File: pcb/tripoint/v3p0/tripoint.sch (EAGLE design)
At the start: 68 parts, among them J2 TC2030-JLINK-NL, T1 HHM1595A1, U1 STM32F091CC, U2 DW1000, U3 SKY13317, U4 LXDC2HN18A, X1 38.4M, X2 16M

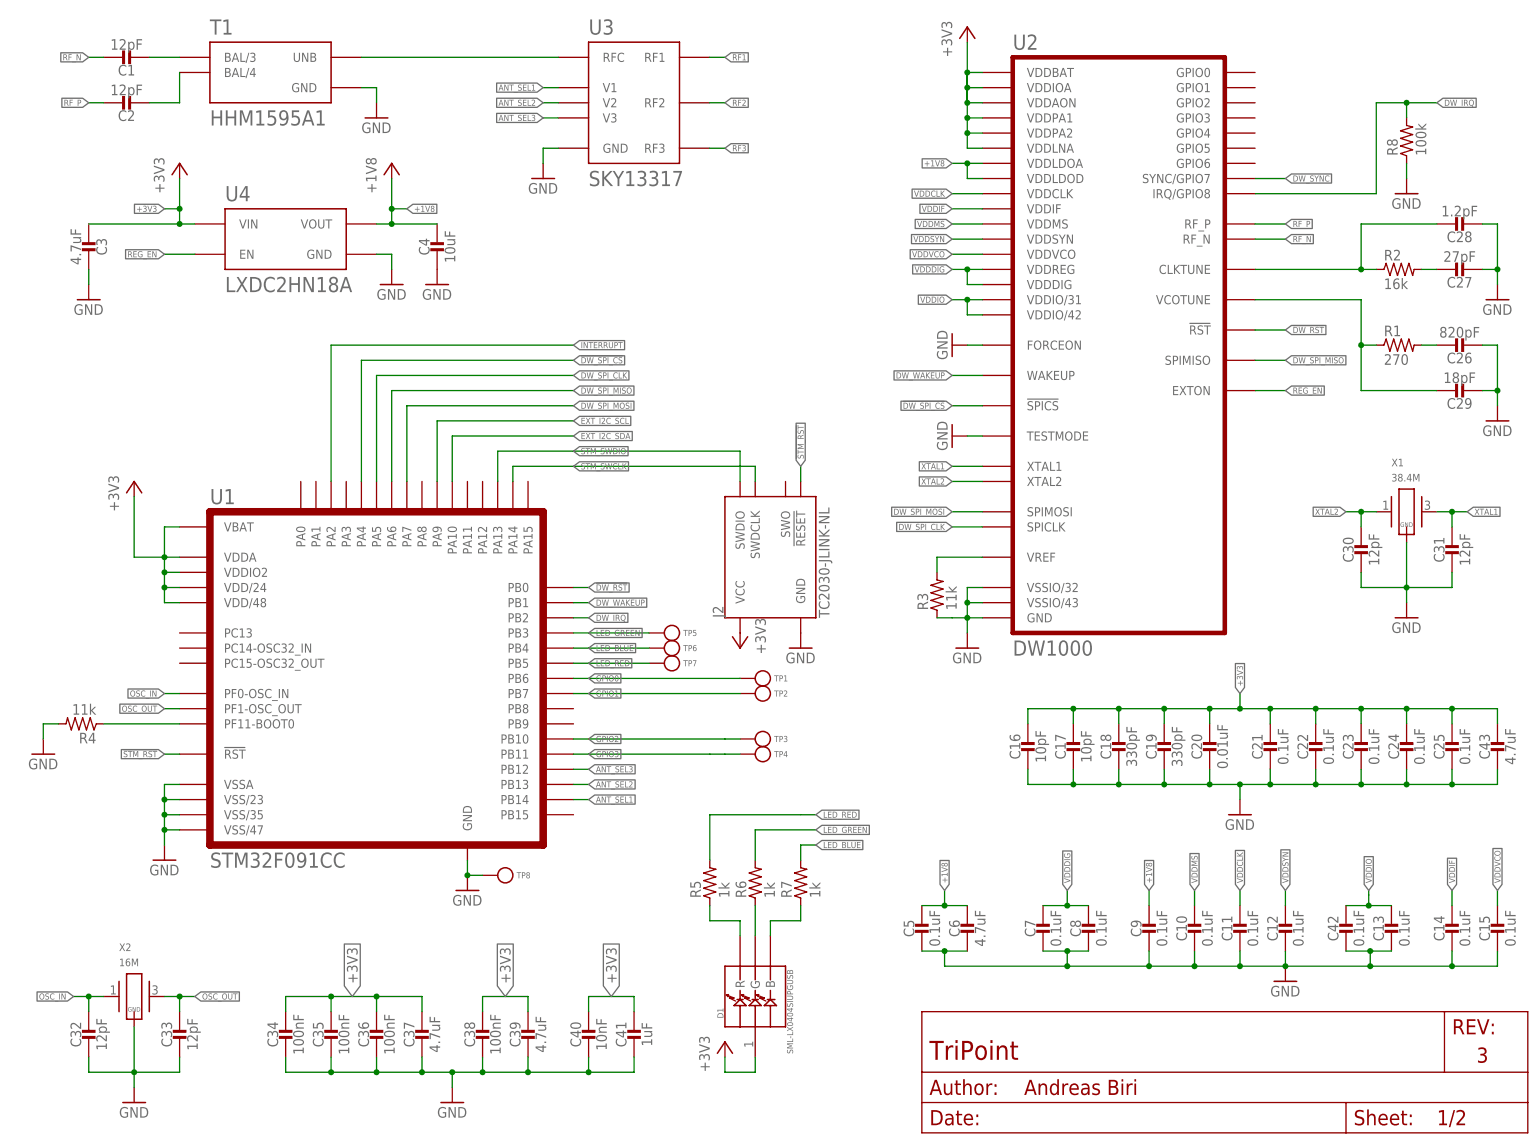
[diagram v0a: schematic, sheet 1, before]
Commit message: added second pass of TriPoint schematic and component positions
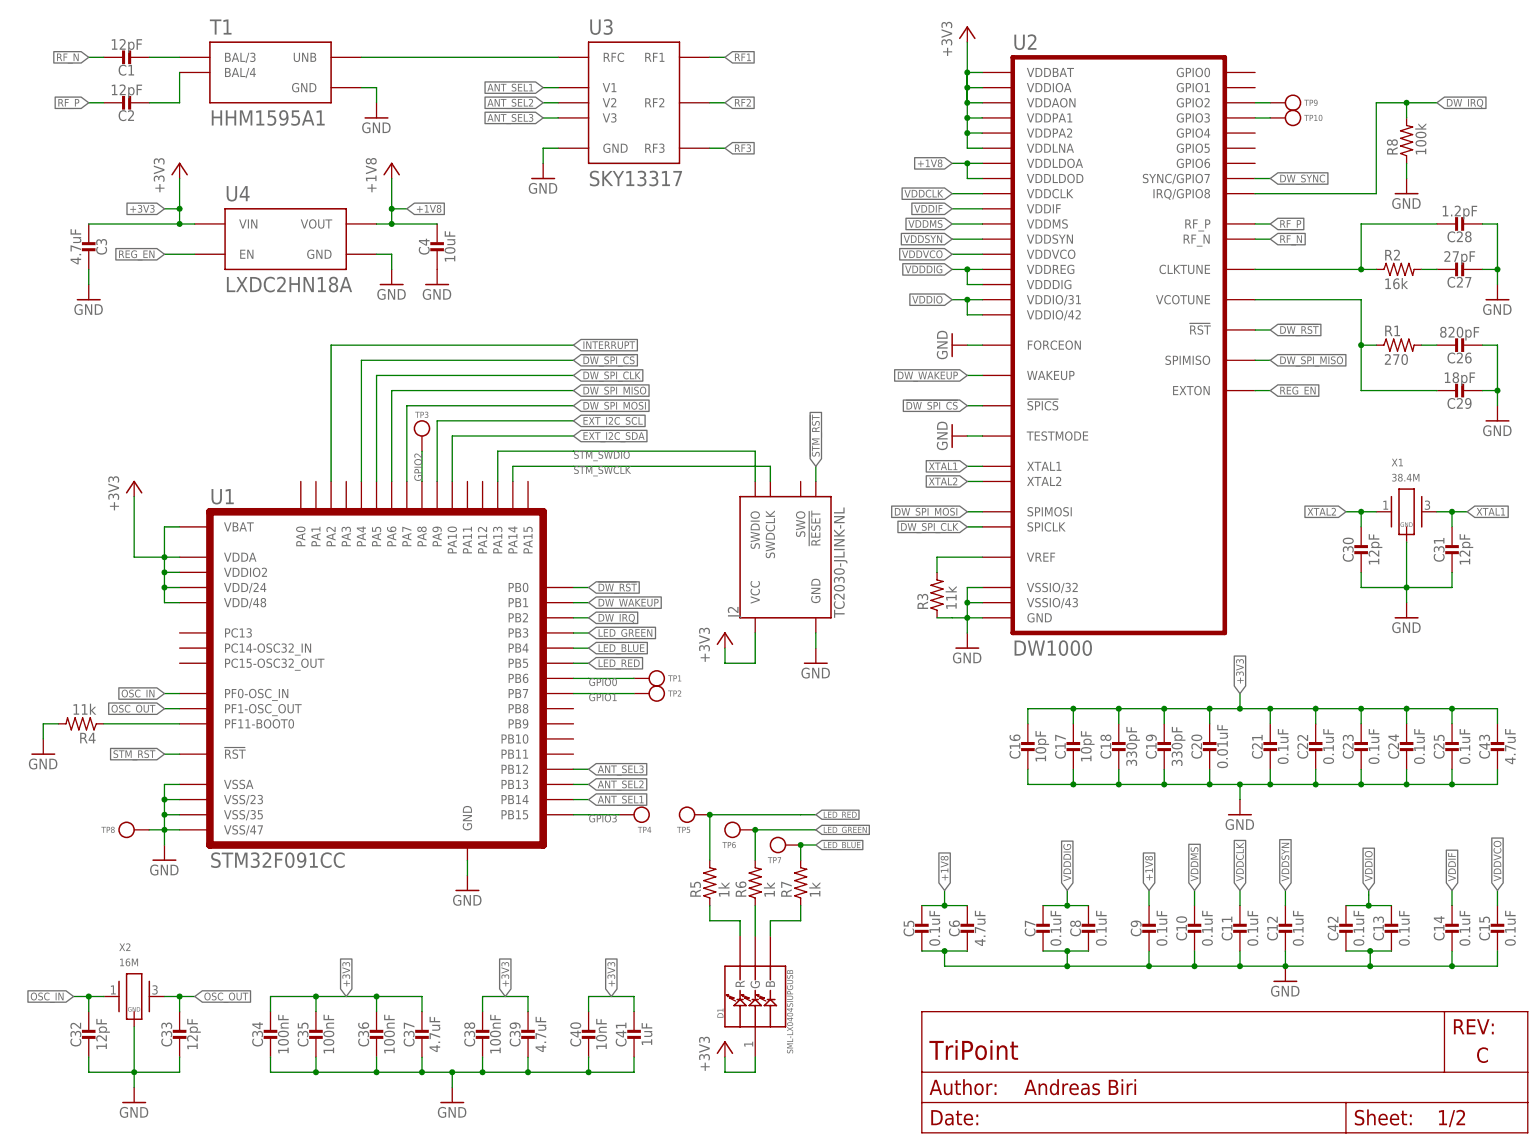
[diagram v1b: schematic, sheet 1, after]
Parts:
- added TP10, TP9: TEST-POINT, headers:TEST-POINT
- C10, C11, C12, C13, C14, C15, C16, C17, C18, C19, C20, C21, C22, C23, C24, C25, C26, C27, C28, C29, C30, C31, C32, C33, C34, C35, C36, C37, C38, C39, C40, C41, C42, C5, C7, C8, C9: device passives:CAPACITOR0201_CAP -> passives:CAPACITOR0402_CAP
- C3, C43, C6: device passives:CAPACITOR0603_CAP -> passives:CAPACITOR0402_CAP
- R1, R2, R3, R4, R8: device passives:RESISTOR0201_RES -> passives:RESISTOR0402_RES
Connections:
- new net N$13: TP9.TESTPOINT, U2.GPIO2
- new net N$14: TP10.TESTPOINT, U2.GPIO3
- net GPIO2: now also U1.PA8; no longer U1.PB10
- net GPIO3: now also U1.PB15; no longer U1.PB11
- net LED_BLUE: now also TP7.TESTPOINT; no longer TP6.TESTPOINT
- net LED_GREEN: now also TP6.TESTPOINT; no longer TP5.TESTPOINT
- net LED_RED: now also TP5.TESTPOINT; no longer TP7.TESTPOINT
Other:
- note added: "Note: Additional I2C pull-up resistors required to +3V3"
- note added: "VDD/24"
- note added: "VDD/48"
- note removed: "Note: Additional I2C pull-up resistors required"
- note removed: "VDD"
- moved on the sheet: C34, C35, J2, TP1, TP2, TP3, TP4, TP5, TP6, TP7, TP8

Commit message: finished second pass of TriPoint
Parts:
- C38: value 100nF -> 4.7uF
- C39: value 4.7uF -> 100nF
- C40: value 10nF -> 1uF
- C41: value 1uF -> 10nF
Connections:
- net LED_BLUE: no longer TP7.TESTPOINT
- net LED_GREEN: now also U1.PB5; no longer TP6.TESTPOINT, U1.PB3
- net LED_RED: now also U1.PB3; no longer TP5.TESTPOINT, U1.PB5
- net N$10: now also TP5.TESTPOINT
- net N$11: now also TP7.TESTPOINT
- net N$12: now also TP6.TESTPOINT
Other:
- moved on the sheet: R5, R6, R7, TP5, TP6, TP7
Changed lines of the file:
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@@
 <part name="C36" library="passives" deviceset="CAPACITOR" device="0402_CAP" value="100nF"/>
 <part name="C37" library="passives" deviceset="CAPACITOR" device="0402_CAP" value="4.7uF"/>
-<part name="C38" library="passives" deviceset="CAPACITOR" device="0402_CAP" value="100nF"/>
-<part name="C39" library="passives" deviceset="CAPACITOR" device="0402_CAP" value="4.7uF"/>
-<part name="C40" library="passives" deviceset="CAPACITOR" device="0402_CAP" value="10nF"/>
-<part name="C41" library="passives" deviceset="CAPACITOR" device="0402_CAP" value="1uF"/>
+<part name="C38" library="passives" deviceset="CAPACITOR" device="0402_CAP" value="4.7uF"/>
+<part name="C39" library="passives" deviceset="CAPACITOR" device="0402_CAP" value="100nF"/>
+<part name="C40" library="passives" deviceset="CAPACITOR" device="0402_CAP" value="1uF"/>
+<part name="C41" library="passives" deviceset="CAPACITOR" device="0402_CAP" value="10nF"/>
 <part name="SUPPLY19" library="regulators" deviceset="GND" device=""/>
 <part name="R4" library="passives" deviceset="RESISTOR" device="0402_RES" value="11k"/>
@@
 <text x="114.3" y="73.66" size="0.762" layer="98">PC
 Test Points</text>
-<text x="114.808" y="56.134" size="0.762" layer="98">Pad
+<text x="101.6" y="47.498" size="0.762" layer="98">Pad
 Test Points</text>
 <text x="129.54" y="30.48" size="2.032" layer="98">LED</text>
@@
 <instance part="SUPPLY22" gate="G1" x="134.62" y="78.74"/>
 <instance part="+3V4" gate="P1" x="119.38" y="83.82"/>
-<instance part="R5" gate="G$1" x="116.84" y="43.18" rot="R90"/>
-<instance part="R6" gate="G$1" x="124.46" y="43.18" rot="R90"/>
+<instance part="R5" gate="G$1" x="114.3" y="50.8" rot="R90"/>
+<instance part="R6" gate="G$1" x="124.46" y="50.8" rot="R90"/>
 <instance part="D1" gate="G$1" x="124.46" y="22.86" rot="R90"/>
-<instance part="R7" gate="G$1" x="132.08" y="43.18" rot="R90"/>
+<instance part="R7" gate="G$1" x="134.62" y="50.8" rot="R90"/>
 <instance part="TP1" gate="G$1" x="106.68" y="76.2" rot="R180"/>
 <instance part="TP2" gate="G$1" x="106.68" y="73.66" rot="R180"/>
@@
 <instance part="C42" gate="G$1" x="223.52" y="35.56"/>
 <instance part="C43" gate="G$1" x="248.92" y="66.04"/>
-<instance part="TP5" gate="G$1" x="114.3" y="53.34" smashed="yes">
-<attribute name="NAME" x="113.665" y="50.8" size="1.016" layer="95" ratio="12" align="center-right"/>
+<instance part="TP5" gate="G$1" x="129.54" y="40.64" smashed="yes" rot="R180">
+<attribute name="NAME" x="130.175" y="38.1" size="1.016" layer="95" ratio="12" rot="R180" align="center-right"/>
 </instance>
-<instance part="TP6" gate="G$1" x="121.92" y="50.8" smashed="yes">
-<attribute name="NAME" x="121.285" y="48.26" size="1.016" layer="95" ratio="12" align="center-right"/>
+<instance part="TP6" gate="G$1" x="119.38" y="40.64" smashed="yes" rot="R180">
+<attribute name="NAME" x="120.015" y="38.1" size="1.016" layer="95" ratio="12" rot="R180" align="center-right"/>
 </instance>
-<instance part="TP7" gate="G$1" x="129.54" y="48.26" smashed="yes">
-<attribute name="NAME" x="128.905" y="45.72" size="1.016" layer="95" ratio="12" align="center-right"/>
+<instance part="TP7" gate="G$1" x="139.7" y="40.64" smashed="yes" rot="R180">
+<attribute name="NAME" x="140.335" y="38.1" size="1.016" layer="95" ratio="12" rot="R180" align="center-right"/>
 </instance>
 <instance part="TP8" gate="G$1" x="20.32" y="50.8"/>
@@
 <pinref part="R6" gate="G$1" pin="1"/>
 <pinref part="D1" gate="G$1" pin="G"/>
-<wire x1="124.46" y1="38.1" x2="124.46" y2="33.02" width="0.1524" layer="91"/>
+<wire x1="124.46" y1="45.72" x2="124.46" y2="40.64" width="0.1524" layer="91"/>
+<pinref part="TP5" gate="G$1" pin="TESTPOINT"/>
+<wire x1="124.46" y1="40.64" x2="124.46" y2="33.02" width="0.1524" layer="91"/>
+<wire x1="127" y1="40.64" x2="124.46" y2="40.64" width="0.1524" layer="91"/>
+<junction x="124.46" y="40.64"/>
 </segment>
 </net>
@@
 <segment>
 <pinref part="R7" gate="G$1" pin="1"/>
-<wire x1="132.08" y1="38.1" x2="132.08" y2="35.56" width="0.1524" layer="91"/>
-<wire x1="132.08" y1="35.56" x2="127" y2="35.56" width="0.1524" layer="91"/>
+<wire x1="134.62" y1="45.72" x2="134.62" y2="40.64" width="0.1524" layer="91"/>
+<wire x1="134.62" y1="40.64" x2="134.62" y2="35.56" width="0.1524" layer="91"/>
+<wire x1="134.62" y1="35.56" x2="127" y2="35.56" width="0.1524" layer="91"/>
 <pinref part="D1" gate="G$1" pin="B"/>
 <wire x1="127" y1="35.56" x2="127" y2="33.02" width="0.1524" layer="91"/>
+<pinref part="TP7" gate="G$1" pin="TESTPOINT"/>
+<wire x1="137.16" y1="40.64" x2="134.62" y2="40.64" width="0.1524" layer="91"/>
+<junction x="134.62" y="40.64"/>
 </segment>
 </net>
@@
 <segment>
 <pinref part="R5" gate="G$1" pin="1"/>
-<wire x1="116.84" y1="38.1" x2="116.84" y2="35.56" width="0.1524" layer="91"/>
-<wire x1="116.84" y1="35.56" x2="121.92" y2="35.56" width="0.1524" layer="91"/>
+<wire x1="114.3" y1="45.72" x2="114.3" y2="40.64" width="0.1524" layer="91"/>
+<wire x1="114.3" y1="40.64" x2="114.3" y2="35.56" width="0.1524" layer="91"/>
+<wire x1="114.3" y1="35.56" x2="121.92" y2="35.56" width="0.1524" layer="91"/>
 <pinref part="D1" gate="G$1" pin="R"/>
 <wire x1="121.92" y1="35.56" x2="121.92" y2="33.02" width="0.1524" layer="91"/>
+<pinref part="TP6" gate="G$1" pin="TESTPOINT"/>
+<wire x1="116.84" y1="40.64" x2="114.3" y2="40.64" width="0.1524" layer="91"/>
+<junction x="114.3" y="40.64"/>
 </segment>
 </net>
@@
 <net name="LED_RED" class="0">
 <segment>
+<wire x1="132.08" y1="60.96" x2="134.62" y2="60.96" width="0.1524" layer="91"/>
+<label x="134.62" y="60.96" size="1.016" layer="95" xref="yes"/>
 <pinref part="R5" gate="G$1" pin="2"/>
-<wire x1="116.84" y1="45.72" x2="116.84" y2="53.34" width="0.1524" layer="91"/>
-<wire x1="116.84" y1="53.34" x2="132.08" y2="53.34" width="0.1524" layer="91"/>
-<wire x1="132.08" y1="53.34" x2="134.62" y2="53.34" width="0.1524" layer="91"/>
-<label x="134.62" y="53.34" size="1.016" layer="95" xref="yes"/>
-<pinref part="TP5" gate="G$1" pin="TESTPOINT"/>
-<junction x="116.84" y="53.34"/>
-</segment>
+<wire x1="114.3" y1="53.34" x2="114.3" y2="60.96" width="0.1524" layer="91"/>
+<wire x1="114.3" y1="60.96" x2="132.08" y2="60.96" width="0.1524" layer="91"/>
+</segment>
+<segment>
+<pinref part="U1" gate="U1" pin="PB3"/>
+<wire x1="93.98" y1="83.82" x2="96.52" y2="83.82" width="0.1524" layer="91"/>
+<label x="96.52" y="83.82" size="1.27" layer="95" xref="yes"/>
+</segment>
+</net>
+<net name="LED_BLUE" class="0">
+<segment>
+<pinref part="U1" gate="U1" pin="PB4"/>
+<wire x1="93.98" y1="81.28" x2="96.52" y2="81.28" width="0.1524" layer="91"/>
+<label x="96.52" y="81.28" size="1.27" layer="95" xref="yes"/>
+</segment>
+<segment>
+<pinref part="R7" gate="G$1" pin="2"/>
+<wire x1="134.62" y1="53.34" x2="134.62" y2="55.88" width="0.1524" layer="91"/>
+<label x="134.62" y="55.88" size="1.016" layer="95" xref="yes"/>
+</segment>
+</net>
+<net name="LED_GREEN" class="0">
 <segment>
 <pinref part="U1" gate="U1" pin="PB5"/>
@@
 <label x="96.52" y="78.74" size="1.27" layer="95" xref="yes"/>
 </segment>
-</net>
-<net name="LED_BLUE" class="0">
-<segment>
-<pinref part="R7" gate="G$1" pin="2"/>
-<wire x1="132.08" y1="45.72" x2="132.08" y2="48.26" width="0.1524" layer="91"/>
-<wire x1="132.08" y1="48.26" x2="134.62" y2="48.26" width="0.1524" layer="91"/>
-<label x="134.62" y="48.26" size="1.016" layer="95" xref="yes"/>
-<pinref part="TP7" gate="G$1" pin="TESTPOINT"/>
-<junction x="132.08" y="48.26"/>
-</segment>
-<segment>
-<pinref part="U1" gate="U1" pin="PB4"/>
-<wire x1="93.98" y1="81.28" x2="96.52" y2="81.28" width="0.1524" layer="91"/>
-<label x="96.52" y="81.28" size="1.27" layer="95" xref="yes"/>
-</segment>
-</net>
-<net name="LED_GREEN" class="0">
 <segment>
 <pinref part="R6" gate="G$1" pin="2"/>
-<wire x1="124.46" y1="45.72" x2="124.46" y2="50.8" width="0.1524" layer="91"/>
-<wire x1="124.46" y1="50.8" x2="134.62" y2="50.8" width="0.1524" layer="91"/>
-<label x="134.62" y="50.8" size="1.016" layer="95" xref="yes"/>
-<pinref part="TP6" gate="G$1" pin="TESTPOINT"/>
-<junction x="124.46" y="50.8"/>
-</segment>
-<segment>
-<pinref part="U1" gate="U1" pin="PB3"/>
-<wire x1="93.98" y1="83.82" x2="96.52" y2="83.82" width="0.1524" layer="91"/>
-<label x="96.52" y="83.82" size="1.27" layer="95" xref="yes"/>
-</segment>
-</net>
+<wire x1="124.46" y1="53.34" x2="124.46" y2="58.42" width="0.1524" layer="91"/>
+<wire x1="124.46" y1="58.42" x2="134.62" y2="58.42" width="0.1524" layer="91"/>
+<label x="134.62" y="58.42" size="1.016" layer="95" xref="yes"/>
+</segment>
+</net>

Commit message: finished third pass, SquarePoint it is
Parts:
- R3: value 11k -> 11k 1%
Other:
- note added: "Antennas"
- note added: "Be aware that the DecaWave is very sensitive regarding its power supply. We suggest using the "MAX8887EZK33+T" from Maxim Integrated. You can find a reference layout at github.com/lab11/polypoint/pcb/tritag."
- note added: "Guarantee 120° offset in-between antennas to maximize polarization difference and antenna diversity RF traces should respect the keepout zones and be surrounded by a via shield. Furthermore, try to keep them as short and straight as possible"
- note added: "Power Supply"
- note added: "Signals"
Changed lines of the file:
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@@
 <part name="R1" library="passives" deviceset="RESISTOR" device="0402_RES" value="270"/>
 <part name="R2" library="passives" deviceset="RESISTOR" device="0402_RES" value="16k"/>
-<part name="R3" library="passives" deviceset="RESISTOR" device="0402_RES" value="11k"/>
+<part name="R3" library="passives" deviceset="RESISTOR" device="0402_RES" value="11k 1%"/>
 <part name="C26" library="passives" deviceset="CAPACITOR" device="0402_CAP" value="820pF"/>
 <part name="C27" library="passives" deviceset="CAPACITOR" device="0402_CAP" value="27pF"/>
@@
 <text x="35.56" y="149.86" size="2.54" layer="98">The following signals must be integrated into all designs using the design block:</text>
 <text x="86.36" y="134.62" size="2.54" layer="98">Note: Additional I2C pull-up resistors required to +3V3</text>
+<text x="78.74" y="60.96" size="2.54" layer="98">Be aware that the DecaWave is very sensitive regarding its power supply.
+We suggest using the "MAX8887EZK33+T" from Maxim Integrated.
+You can find a reference layout at github.com/lab11/polypoint/pcb/tritag.</text>
+<text x="7.62" y="101.6" size="3.556" layer="98">Antennas</text>
+<text x="78.74" y="88.9" size="2.54" layer="98">Guarantee 120° offset in-between antennas to maximize  polarization difference and antenna diversity
+RF traces should respect the keepout zones and be surrounded by a via shield.
+Furthermore, try to keep them as short and straight as possible</text>
+<text x="7.62" y="73.66" size="3.556" layer="98">Power Supply</text>
+<text x="7.62" y="137.16" size="3.556" layer="98">Signals</text>
 </plain>
 <instances>
@@
 <net name="RF1" class="0">
 <segment>
-<wire x1="35.56" y1="109.22" x2="50.8" y2="109.22" width="0.1524" layer="91"/>
-<label x="50.8" y="109.22" size="2.54" layer="95" xref="yes"/>
+<wire x1="35.56" y1="101.6" x2="50.8" y2="101.6" width="0.1524" layer="91"/>
+<label x="50.8" y="101.6" size="2.54" layer="95" xref="yes"/>
 </segment>
 </net>
 <net name="RF2" class="0">
 <segment>
-<wire x1="35.56" y1="104.14" x2="50.8" y2="104.14" width="0.1524" layer="91"/>
-<label x="50.8" y="104.14" size="2.54" layer="95" xref="yes"/>
+<wire x1="35.56" y1="96.52" x2="50.8" y2="96.52" width="0.1524" layer="91"/>
+<label x="50.8" y="96.52" size="2.54" layer="95" xref="yes"/>
 </segment>
 </net>
 <net name="RF3" class="0">
 <segment>
-<wire x1="35.56" y1="99.06" x2="50.8" y2="99.06" width="0.1524" layer="91"/>
-<label x="50.8" y="99.06" size="2.54" layer="95" xref="yes"/>
+<wire x1="35.56" y1="91.44" x2="50.8" y2="91.44" width="0.1524" layer="91"/>
+<label x="50.8" y="91.44" size="2.54" layer="95" xref="yes"/>
 </segment>
 </net>
 <net name="+3V3" class="0">
 <segment>
-<wire x1="35.56" y1="86.36" x2="50.8" y2="86.36" width="0.1524" layer="91"/>
-<label x="50.8" y="86.36" size="2.54" layer="95" xref="yes"/>
-</segment>
-</net>
-<net name="+1V8" class="0">
-<segment>
-<wire x1="35.56" y1="81.28" x2="50.8" y2="81.28" width="0.1524" layer="91"/>
-<label x="50.8" y="81.28" size="2.54" layer="95" xref="yes"/>
-</segment>
-</net>
+<wire x1="35.56" y1="71.12" x2="50.8" y2="71.12" width="0.1524" layer="91"/>
+<label x="50.8" y="71.12" size="2.54" layer="95" xref="yes"/>
+</segment>
+</net>
